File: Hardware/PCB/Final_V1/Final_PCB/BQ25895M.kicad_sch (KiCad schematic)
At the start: 20 parts, among them IC1 BQ25895MRTWT

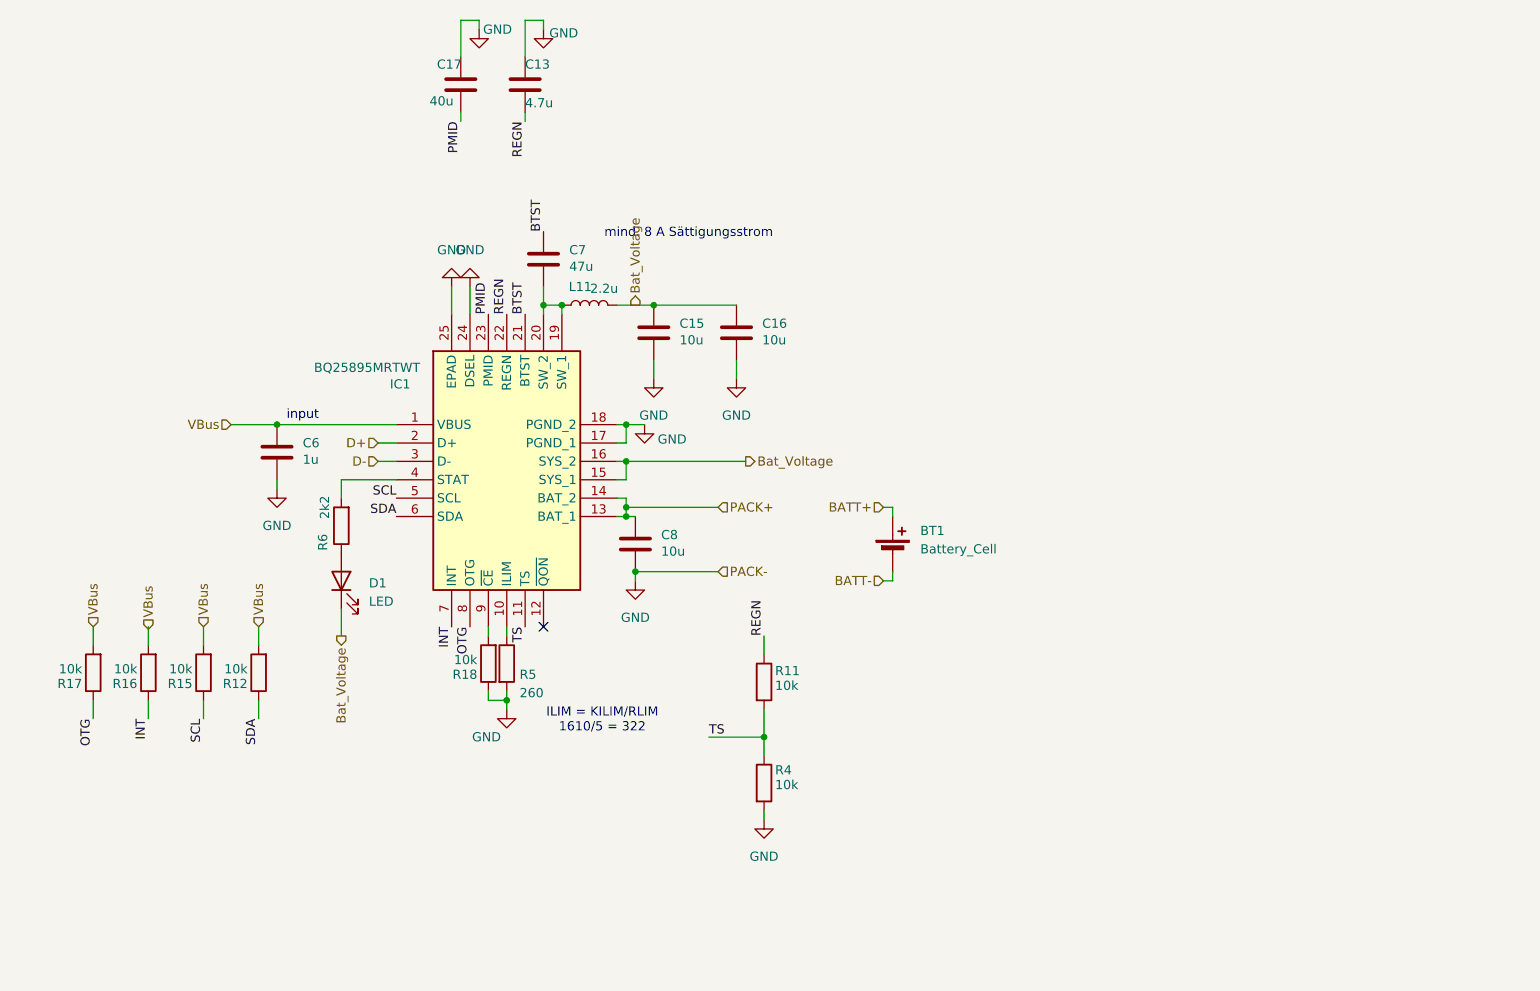
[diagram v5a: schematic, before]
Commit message: fixed some minor mistakes and added test pads for the battery charger
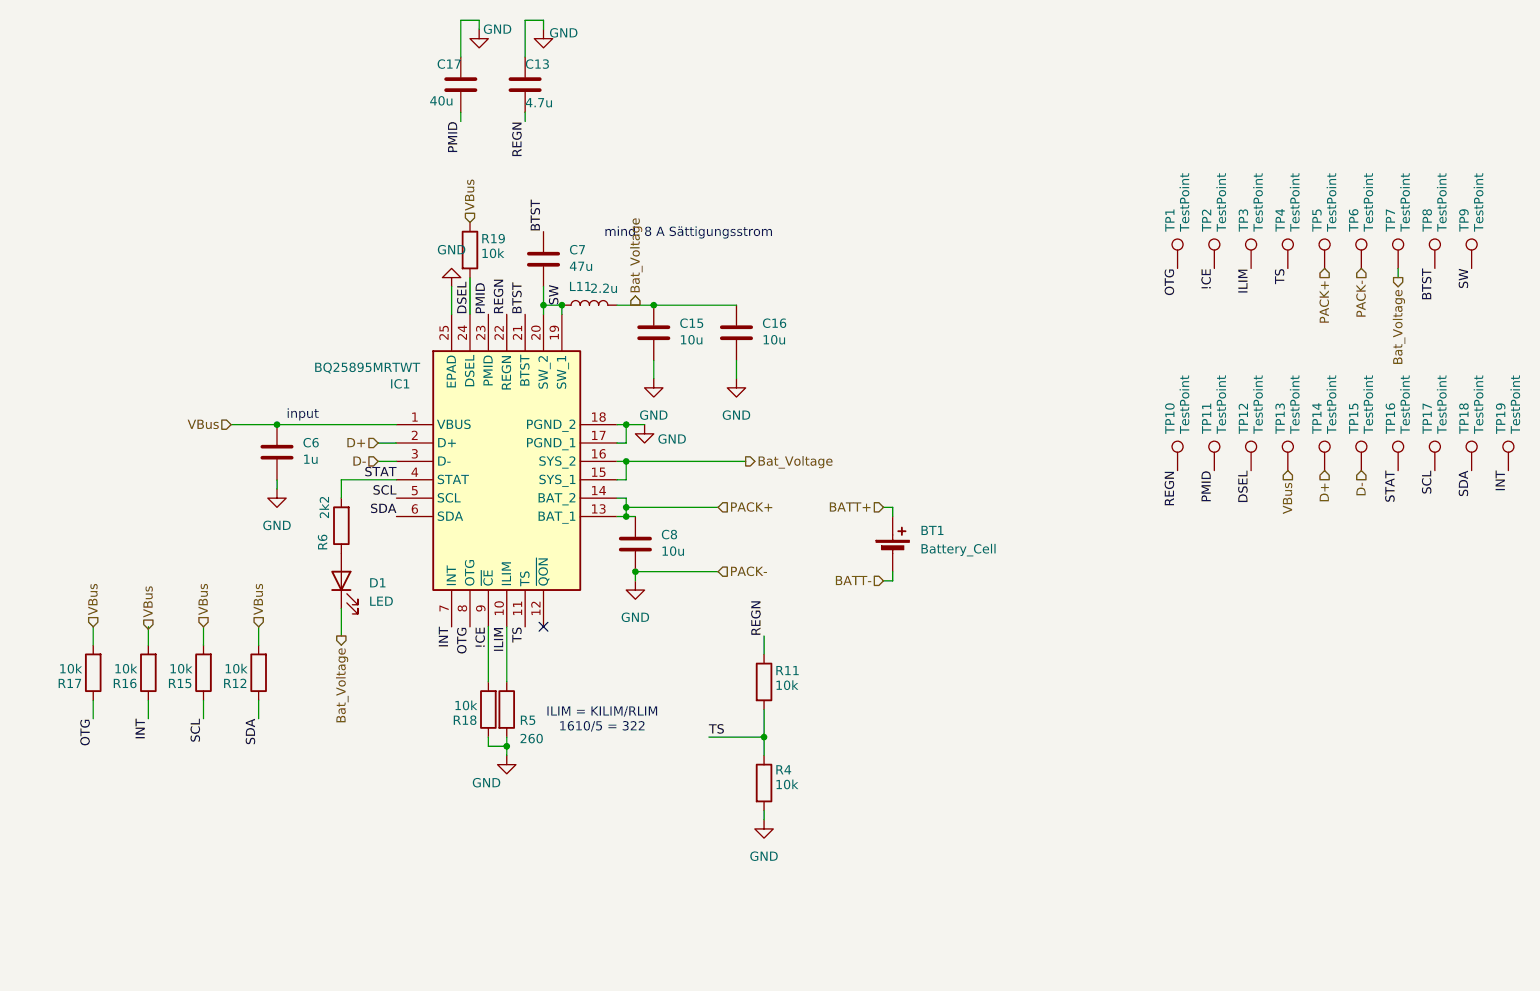
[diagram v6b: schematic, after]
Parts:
- added R19: 10k, Resistor_SMD:R_0603_1608Metric, symbol Device:R
- added TP1, TP10, TP11, TP12, TP13, TP14, TP15, TP16, TP17, TP18, TP19, TP2, TP3, TP4, TP5, TP6, TP7, TP8, TP9: TestPoint, TestPoint:TestPoint_Pad_1.5x1.5mm, symbol Connector:TestPoint
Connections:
- net BTST: now also TP8.1
- net Bat_Voltage: now also TP7.1
- net D+: now also TP14.1
- net D-: now also TP15.1
- net GND: now also TP6.1; no longer IC1.24 (DSEL)
- net INT: now also TP19.1
- net OTG: now also TP1.1
- net PACK+: now also TP5.1
- net PMID: now also TP11.1
- net REGN: now also TP10.1
- net SCL: now also TP17.1
- net SDA: now also TP18.1
- net TS: now also TP4.1
- net VBus: now also R19.1, TP13.1
- net ILIM: now reaches IC1.10 (ILIM), R5.1
- net ILIM: now also TP3.1
- net SW: now reaches C7.2, IC1.19 (SW_1), IC1.20 (SW_2), L11.1
- net SW: now also TP9.1
- net STAT: now reaches IC1.4 (STAT), R6.2
- net STAT: now also TP16.1
- net !CE: now reaches IC1.9 (~{CE}), R18.2
- net !CE: now also TP2.1
- new net DSEL: IC1.24 (DSEL), R19.2, TP12.1
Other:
- moved on the sheet: R18, R5

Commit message: #4: Layout-Session-17-11-25
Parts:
- BT1: footprint (none) -> Connector_PinHeader_2.54mm:PinHeader_1x02_P2.54mm_Vertical
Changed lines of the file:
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@@
 			)
 		)
-		(property "Footprint" ""
+		(property "Footprint" "Connector_PinHeader_2.54mm:PinHeader_1x02_P2.54mm_Vertical"
 			(at 184.15 101.346 90)
 			(effects

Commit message: a few pcb edits
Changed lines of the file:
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@@
-	(wire
-		(pts
-			(xy 81.28 115.57) (xy 81.28 113.03)
-		)
-		(stroke
-			(width 0)
-			(type default)
-		)
-	)
 	(wire
 		(pts
@@
 		(pts
 			(xy 124.46 34.29) (xy 124.46 29.21)
+		)
+		(stroke
+			(width 0)
+			(type default)
+		)
+	)
+	(wire
+		(pts
+			(xy 81.28 113.03) (xy 81.28 115.57)
 		)
 		(stroke
@@
 	(hierarchical_label "VBus"
 		(shape input)
-		(at 81.28 113.3627 90)
-		(effects
-			(font
+		(at 81.28 113.03 90)
+		(effects
+			(font
